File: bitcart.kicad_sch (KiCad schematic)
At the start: 8 parts

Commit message: removed many unused parts
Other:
- company: © 2020-2022 Raspberry Pi Ltd (formerly Raspberry Pi (Trading) Ltd.) -> (none)
- title: Compute Module 4 IO Board - Top Level -> bitcart - Top Level

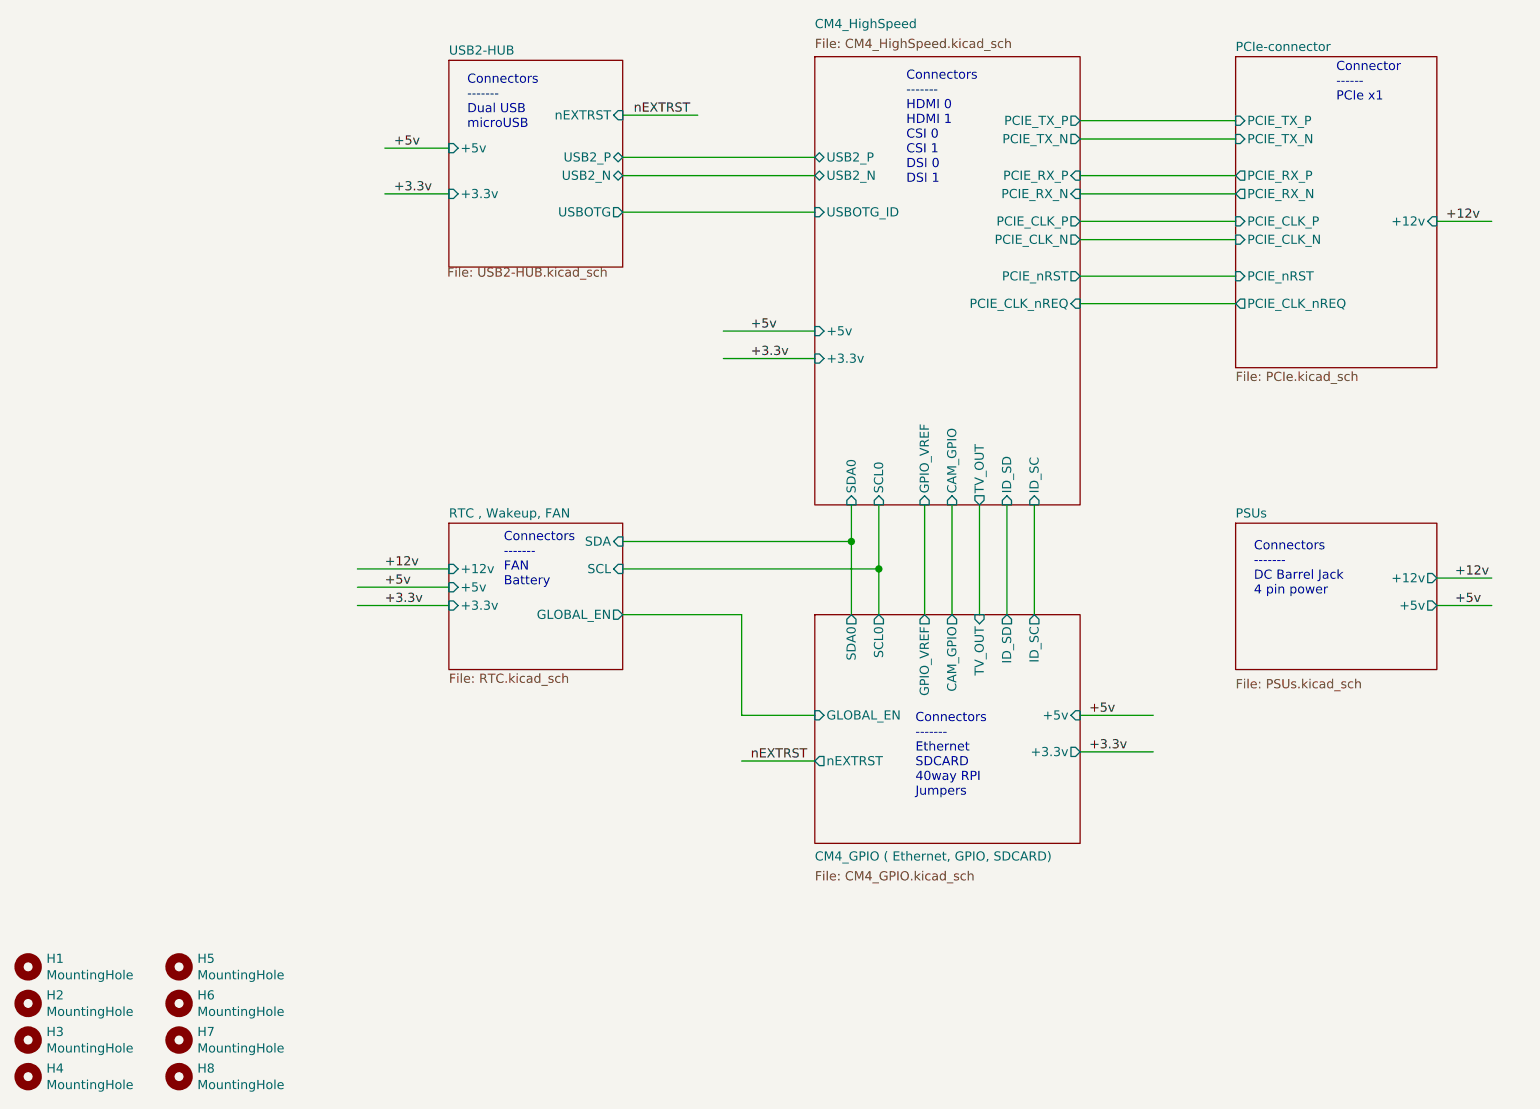
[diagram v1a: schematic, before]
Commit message: added PoE schematic
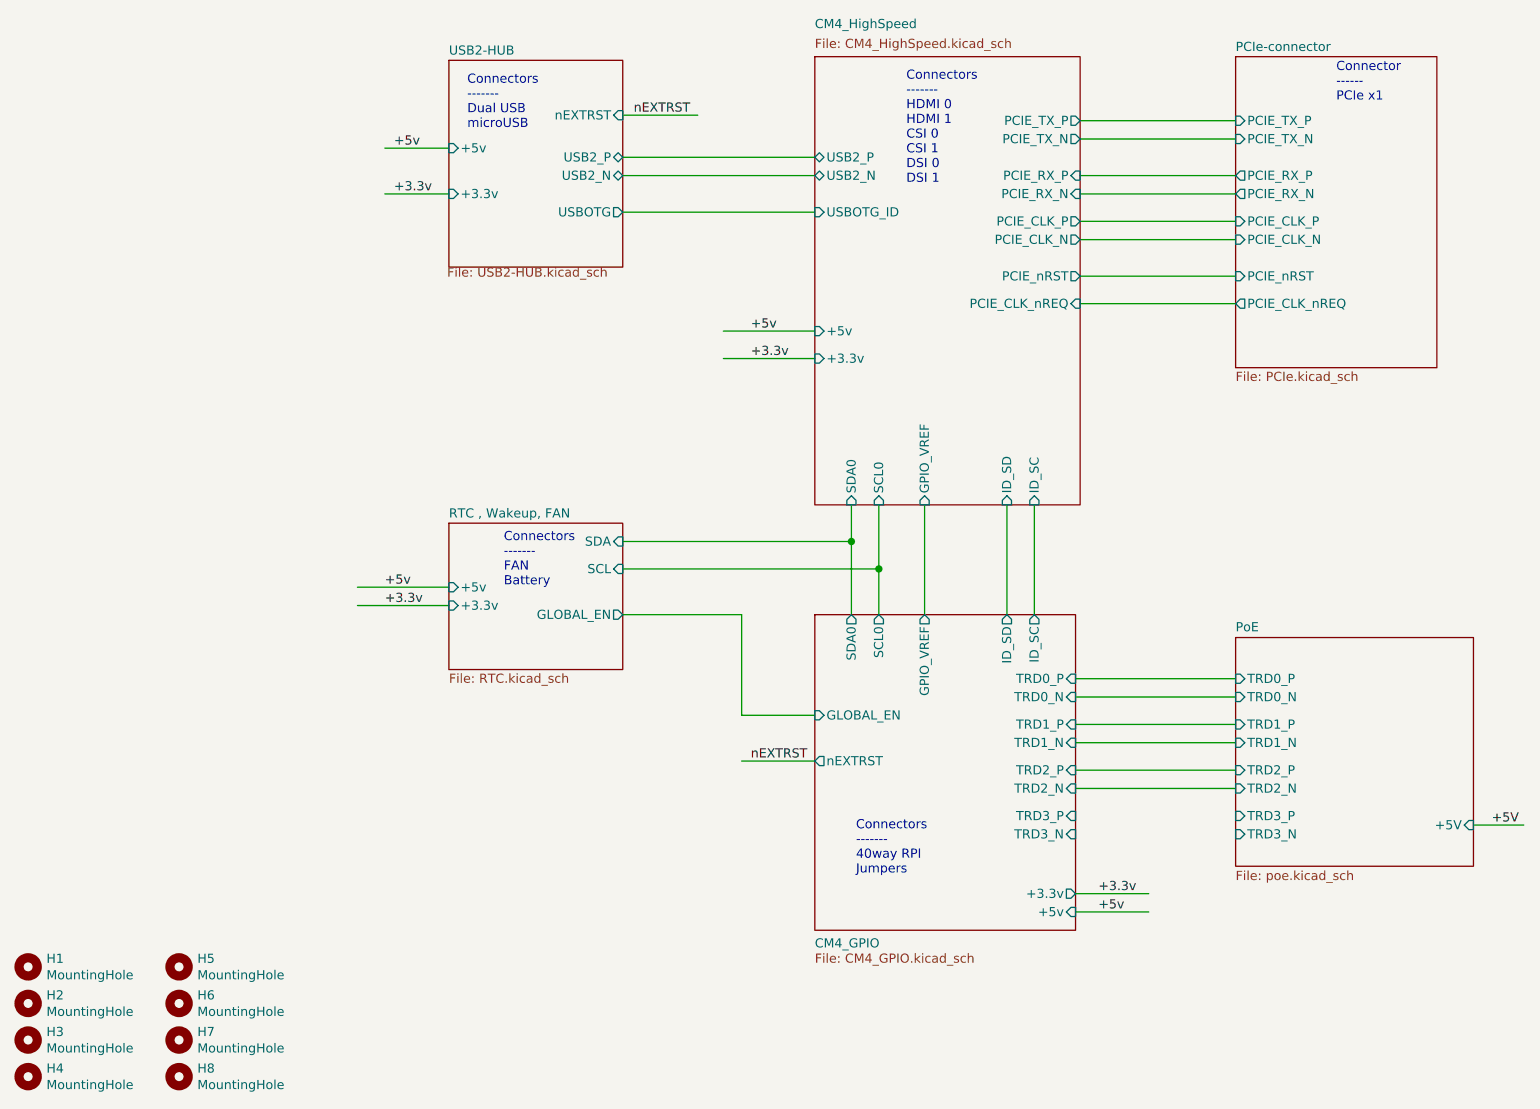
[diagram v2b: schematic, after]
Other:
- sheet CM4_GPIO ( Ethernet, GPIO, SDCARD) renamed CM4_GPIO 
- removed sheet PSUs
- added sheet PoE (poe.kicad_sch)
- sheet CM4_GPIO  ports: added TRD0_N, TRD0_P, TRD1_N, TRD1_P, TRD2_N, TRD2_P, TRD3_N, TRD3_P; removed CAM_GPIO, TV_OUT
- sheet CM4_HighSpeed ports: added none; removed CAM_GPIO, TV_OUT
- sheet PCIe-connector ports: added none; removed +12v
- sheet RTC , Wakeup, FAN ports: added none; removed +12v
- note added: "Connectors ------- 40way RPI Jumpers"
- note removed: "Connectors ------- DC Barrel Jack 4 pin power"
- note removed: "Connectors ------- Ethernet SDCARD 40way RPI Jumpers"

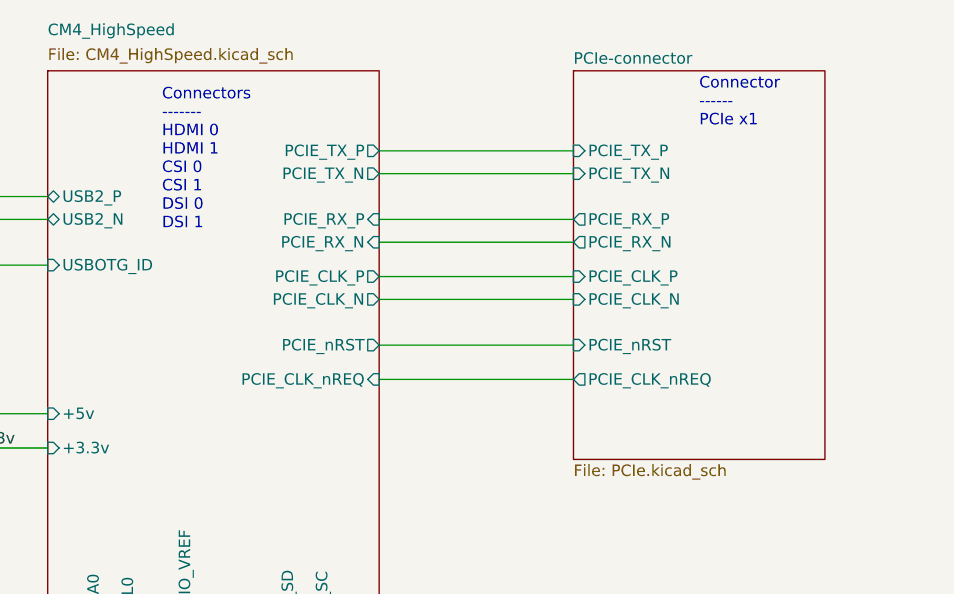
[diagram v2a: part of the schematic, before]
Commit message: added M.2 m-key connector to schematic
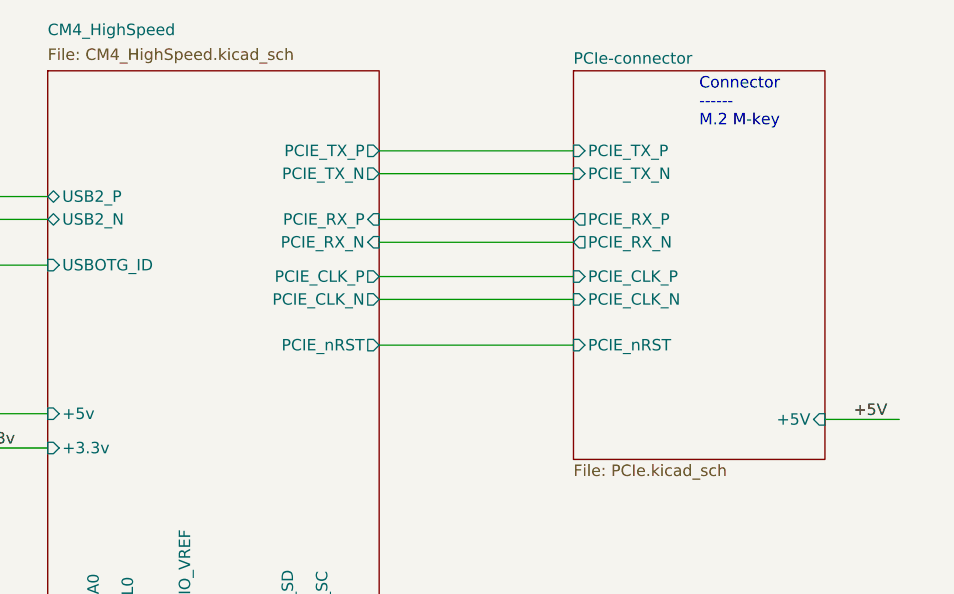
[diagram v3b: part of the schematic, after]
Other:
- sheet CM4_HighSpeed ports: added none; removed PCIE_CLK_nREQ
- sheet PCIe-connector ports: added +5V; removed PCIE_CLK_nREQ
- note added: "Connector ------ M.2 M-key"
- note removed: "Connector ------ PCIe x1"
- note removed: "Connectors ------- HDMI 0 HDMI 1 CSI 0 CSI 1 DSI 0 DSI 1"

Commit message: schematic cleanup
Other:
- sheet RTC , Wakeup, FAN renamed FAN
- sheet CM4_GPIO  ports: added none; removed GPIO_VREF
- sheet CM4_HighSpeed ports: added none; removed GPIO_VREF, SCL0, SDA0
- note added: "Connectors ------- FAN"
- note added: "Connectors ------- microUSB"
- note removed: "Connectors ------- Dual USB microUSB"
- note removed: "Connectors ------- FAN Battery"
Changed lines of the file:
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@@
     (comment 1 "https://github.com/skot/bitcart.git")
   )
-  (junction (at 140.97 110.49) (diameter 1.016) (color 0 0 0 0)
-  )
-  (junction (at 137.16 106.68) (diameter 1.016) (color 0 0 0 0)
-  )
   (wire (pts (xy 81.28 52.07) (xy 72.39 52.07))
     (stroke (width 0) (type solid) (color 0 0 0 0))
@@
     (stroke (width 0) (type solid) (color 0 0 0 0))
   )
+  (wire (pts (xy 168.275 144.78) (xy 190.5 144.78))
+    (stroke (width 0) (type default) (color 0 0 0 0))
+  )
   (wire (pts (xy 168.91 69.85) (xy 190.5 69.85))
     (stroke (width 0) (type solid) (color 0 0 0 0))
   )
-  (wire (pts (xy 137.16 101.6) (xy 137.16 106.68))
-    (stroke (width 0) (type solid) (color 0 0 0 0))
+  (wire (pts (xy 106.68 124.46) (xy 132.08 124.46))
+    (stroke (width 0) (type default) (color 0 0 0 0))
   )
   (wire (pts (xy 162.56 116.84) (xy 162.56 101.6))
     (stroke (width 0) (type solid) (color 0 0 0 0))
   )
-  (wire (pts (xy 147.32 101.6) (xy 147.32 116.84))
-    (stroke (width 0) (type solid) (color 0 0 0 0))
-  )
   (wire (pts (xy 105.41 55.88) (xy 132.08 55.88))
     (stroke (width 0) (type solid) (color 0 0 0 0))
   )
-  (wire (pts (xy 140.97 110.49) (xy 140.97 101.6))
-    (stroke (width 0) (type solid) (color 0 0 0 0))
-  )
   (wire (pts (xy 168.275 134.62) (xy 190.5 134.62))
     (stroke (width 0) (type default) (color 0 0 0 0))
@@
     (stroke (width 0) (type solid) (color 0 0 0 0))
   )
-  (wire (pts (xy 105.41 110.49) (xy 140.97 110.49))
-    (stroke (width 0) (type solid) (color 0 0 0 0))
-  )
-  (wire (pts (xy 137.16 106.68) (xy 137.16 116.84))
-    (stroke (width 0) (type solid) (color 0 0 0 0))
-  )
   (wire (pts (xy 168.275 132.08) (xy 190.5 132.08))
     (stroke (width 0) (type default) (color 0 0 0 0))
@@
     (stroke (width 0) (type solid) (color 0 0 0 0))
   )
+  (wire (pts (xy 168.275 147.32) (xy 190.5 147.32))
+    (stroke (width 0) (type default) (color 0 0 0 0))
+  )
   (wire (pts (xy 119.38 77.47) (xy 132.08 77.47))
     (stroke (width 0) (type solid) (color 0 0 0 0))
@@
     (stroke (width 0) (type solid) (color 0 0 0 0))
   )
-  (wire (pts (xy 105.41 106.68) (xy 137.16 106.68))
-    (stroke (width 0) (type solid) (color 0 0 0 0))
-  )
-  (wire (pts (xy 68.58 113.03) (xy 81.28 113.03))
+  (wire (pts (xy 69.85 127) (xy 82.55 127))
     (stroke (width 0) (type solid) (color 0 0 0 0))
   )
@@
     (stroke (width 0) (type default) (color 0 0 0 0))
   )
+  (wire (pts (xy 106.68 130.81) (xy 132.08 130.81))
+    (stroke (width 0) (type default) (color 0 0 0 0))
+  )
   (wire (pts (xy 168.275 138.43) (xy 190.5 138.43))
     (stroke (width 0) (type default) (color 0 0 0 0))
   )
+  (wire (pts (xy 106.68 120.65) (xy 132.08 120.65))
+    (stroke (width 0) (type default) (color 0 0 0 0))
+  )
   (wire (pts (xy 158.75 101.6) (xy 158.75 116.84))
     (stroke (width 0) (type solid) (color 0 0 0 0))
   )
-  (wire (pts (xy 105.41 116.84) (xy 121.92 116.84))
-    (stroke (width 0) (type solid) (color 0 0 0 0))
-  )
   (wire (pts (xy 168.275 125.73) (xy 190.5 125.73))
     (stroke (width 0) (type default) (color 0 0 0 0))
@@
     (stroke (width 0) (type solid) (color 0 0 0 0))
   )
-  (wire (pts (xy 81.28 115.57) (xy 68.58 115.57))
+  (wire (pts (xy 82.55 129.54) (xy 69.85 129.54))
     (stroke (width 0) (type solid) (color 0 0 0 0))
   )
@@
     (stroke (width 0) (type solid) (color 0 0 0 0))
   )
-  (wire (pts (xy 121.92 130.81) (xy 121.92 116.84))
-    (stroke (width 0) (type solid) (color 0 0 0 0))
-  )
-  (wire (pts (xy 140.97 116.84) (xy 140.97 110.49))
-    (stroke (width 0) (type solid) (color 0 0 0 0))
-  )
-  (wire (pts (xy 132.08 130.81) (xy 121.92 130.81))
-    (stroke (width 0) (type solid) (color 0 0 0 0))
-  )
-  (text "Connectors\n-------\nFAN\nBattery" (at 88.9 113.03 0)
-    (effects (font (size 1.27 1.27)) (justify left bottom))
-  )
-  (text "Connector\n------\nM.2 M-key" (at 204.47 45.72 0)
-    (effects (font (size 1.27 1.27)) (justify left bottom))
-  )
-  (text "Connectors\n-------\nDual USB\nmicroUSB" (at 83.82 49.53 0)
+  (text "Connectors\n-------\nFAN" (at 83.185 125.095 0)
+    (effects (font (size 1.27 1.27)) (justify left bottom))
+  )
+  (text "Connector\n------\nM.2 M-key" (at 191.135 46.355 0)
+    (effects (font (size 1.27 1.27)) (justify left bottom))
+  )
+  (text "Connectors\n-------\nmicroUSB" (at 81.915 46.99 0)
     (effects (font (size 1.27 1.27)) (justify left bottom))
   )
@@
     (effects (font (size 1.27 1.27)) (justify left bottom))
   )
-  (label "+5v" (at 72.39 113.03 0)
+  (label "+5v" (at 73.025 127 0)
     (effects (font (size 1.27 1.27)) (justify left bottom))
   )
@@
     (effects (font (size 1.27 1.27)) (justify left bottom))
   )
-  (label "+3.3v" (at 72.39 115.57 0)
+  (label "+3.3v" (at 73.025 129.54 0)
     (effects (font (size 1.27 1.27)) (justify left bottom))
   )
@@
     (effects (font (size 1.27 1.27)) (justify left bottom))
   )
-  (label "+5V" (at 226.06 146.05 0)
+  (label "+5v" (at 226.06 146.05 0)
     (effects (font (size 1.27 1.27)) (justify left bottom))
   )
@@
     (effects (font (size 1.27 1.27)) (justify left bottom))
   )
-  (label "+5V" (at 221.615 78.105 0)
+  (label "+5v" (at 221.615 78.105 0)
     (effects (font (size 1.27 1.27)) (justify left bottom))
   )
@@
       (effects (font (size 1.27 1.27)) (justify right))
     )
-    (pin "SCL0" output (at 140.97 116.84 90)
-      (effects (font (size 1.27 1.27)) (justify right))
-    )
-    (pin "SDA0" output (at 137.16 116.84 90)
-      (effects (font (size 1.27 1.27)) (justify right))
-    )
     (pin "+5v" input (at 168.275 158.115 0)
       (effects (font (size 1.27 1.27)) (justify right))
@@
       (effects (font (size 1.27 1.27)) (justify left))
     )
-    (pin "GPIO_VREF" output (at 147.32 116.84 90)
-      (effects (font (size 1.27 1.27)) (justify right))
-    )
     (pin "TRD3_P" input (at 168.275 144.78 0)
       (effects (font (size 1.27 1.27)) (justify right))
@@
     (pin "TRD0_N" input (at 168.275 128.27 0)
       (effects (font (size 1.27 1.27)) (justify right))
+    )
+    (pin "SCL0" output (at 132.08 124.46 180)
+      (effects (font (size 1.27 1.27)) (justify left))
+    )
+    (pin "SDA0" output (at 132.08 120.65 180)
+      (effects (font (size 1.27 1.27)) (justify left))
     )
   )
@@
       (effects (font (size 1.27 1.27)) (justify left))
     )
-    (pin "SCL0" input (at 140.97 101.6 270)
-      (effects (font (size 1.27 1.27)) (justify left))
-    )
-    (pin "SDA0" input (at 137.16 101.6 270)
-      (effects (font (size 1.27 1.27)) (justify left))
-    )
     (pin "+5v" input (at 132.08 77.47 180)
       (effects (font (size 1.27 1.27)) (justify left))
@@
     )
     (pin "USBOTG_ID" input (at 132.08 60.96 180)
-      (effects (font (size 1.27 1.27)) (justify left))
-    )
-    (pin "GPIO_VREF" input (at 147.32 101.6 270)
       (effects (font (size 1.27 1.27)) (justify left))
     )
@@
     )
   )
-  (sheet (at 81.28 104.14) (size 24.13 20.32)
+  (sheet (at 82.55 118.11) (size 24.13 20.32)
     (stroke (width 0.1524) (type solid) (color 132 0 132 1))
     (fill (color 255 255 255 0.0000))
-    (property "Sheet name" "RTC , Wakeup, FAN" (id 0) (at 81.28 103.5045 0)
+    (property "Sheet name" "FAN" (id 0) (at 82.55 117.4745 0)
       (effects (font (size 1.27 1.27)) (justify left bottom))
     )
-    (property "Sheet file" "RTC.kicad_sch" (id 1) (at 81.28 124.9685 0)
+    (property "Sheet file" "RTC.kicad_sch" (id 1) (at 82.55 138.9385 0)
       (effects (font (size 1.27 1.27)) (justify left top))
     )
-    (pin "SCL" input (at 105.41 110.49 0)
-      (effects (font (size 1.27 1.27)) (justify right))
-    )
-    (pin "SDA" input (at 105.41 106.68 0)
-      (effects (font (size 1.27 1.27)) (justify right))
-    )
-    (pin "+5v" input (at 81.28 113.03 180)
-      (effects (font (size 1.27 1.27)) (justify left))
-    )
-    (pin "+3.3v" input (at 81.28 115.57 180)
-      (effects (font (size 1.27 1.27)) (justify left))
-    )
-    (pin "GLOBAL_EN" output (at 105.41 116.84 0)
+    (pin "SCL" input (at 106.68 124.46 0)
+      (effects (font (size 1.27 1.27)) (justify right))
+    )
+    (pin "SDA" input (at 106.68 120.65 0)
+      (effects (font (size 1.27 1.27)) (justify right))
+    )
+    (pin "+5v" input (at 82.55 127 180)
+      (effects (font (size 1.27 1.27)) (justify left))
+    )
+    (pin "+3.3v" input (at 82.55 129.54 180)
+      (effects (font (size 1.27 1.27)) (justify left))
+    )
+    (pin "GLOBAL_EN" output (at 106.68 130.81 0)
       (effects (font (size 1.27 1.27)) (justify right))
     )
@@
       (reference "R4") (unit 1) (value "9.31k") (footprint "")
     )
-    (path "/00000000-0000-0000-0000-00005cff706a/00000000-0000-0000-0000-00005e5f44e8"
-      (reference "R5") (unit 1) (value "0R") (footprint "Resistor_SMD:R_0805_2012Metric_Pad1.15x1.40mm_HandSolder")
-    )
     (path "/5ffb3b4b-7652-4af4-839a-2e6de4752496/9281b472-838c-46a5-af5e-28aac8f740e7"

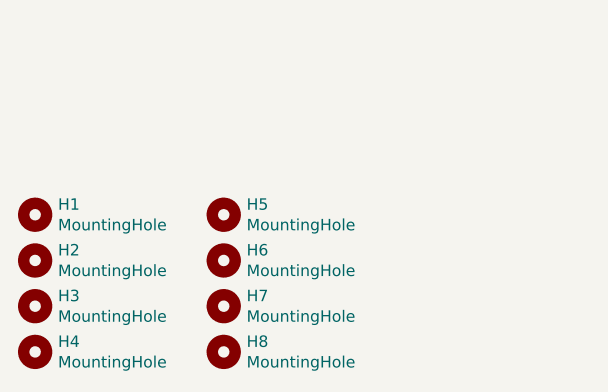
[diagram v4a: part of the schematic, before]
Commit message: removed unused components
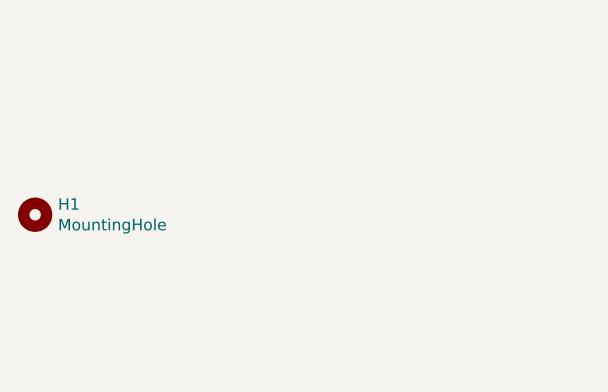
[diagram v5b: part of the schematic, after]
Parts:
- removed H2, H3, H4, H5, H6, H7, H8: MountingHole, MountingHole:MountingHole_2.7mm_M2.5, symbol Mechanical:MountingHole
